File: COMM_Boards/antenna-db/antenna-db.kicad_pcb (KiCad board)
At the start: 4 copper layers, 90.2 x 95.9 mm, 5 parts, among them J1 PC104_Connector

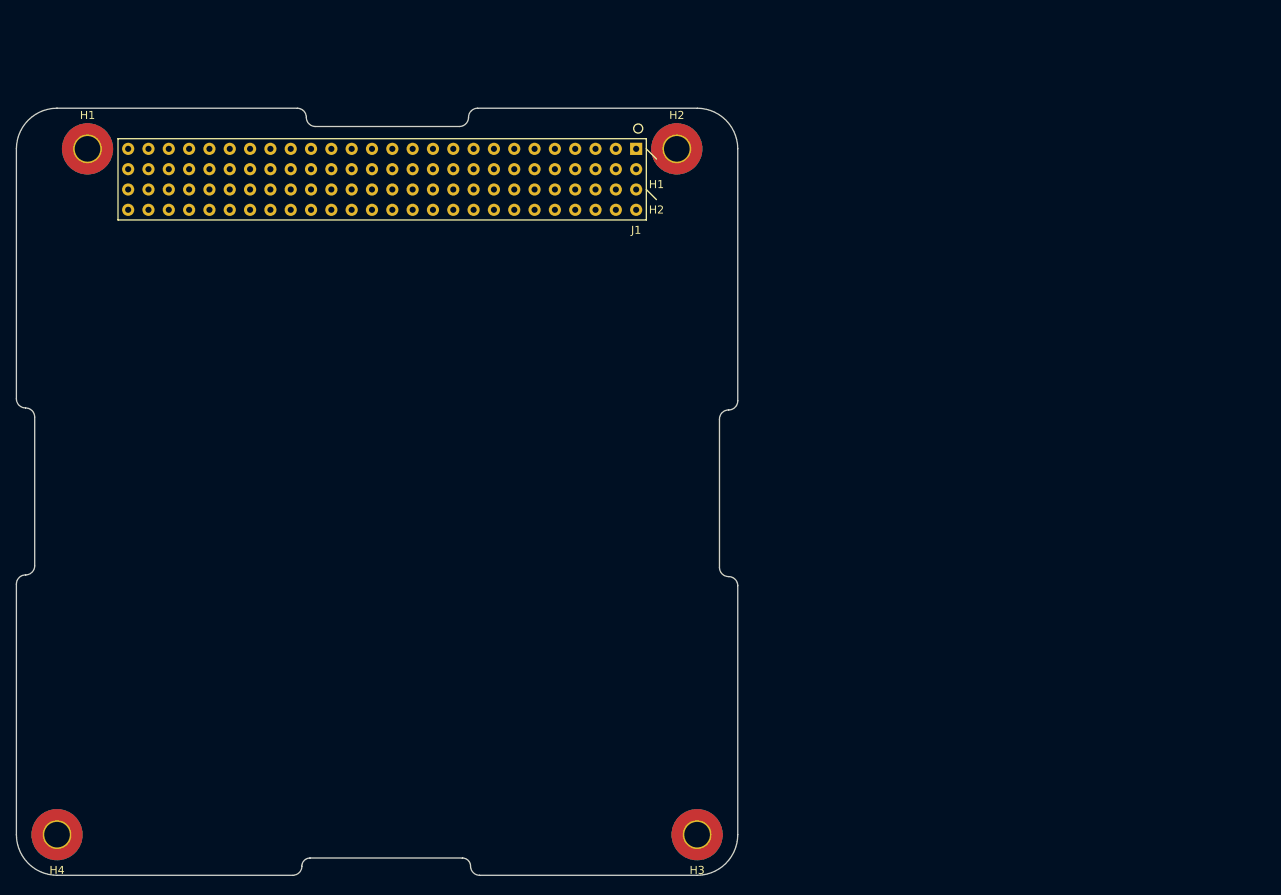
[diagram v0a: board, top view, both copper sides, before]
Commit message: COMM: antt-dbd: map mounting holes to pcb layout
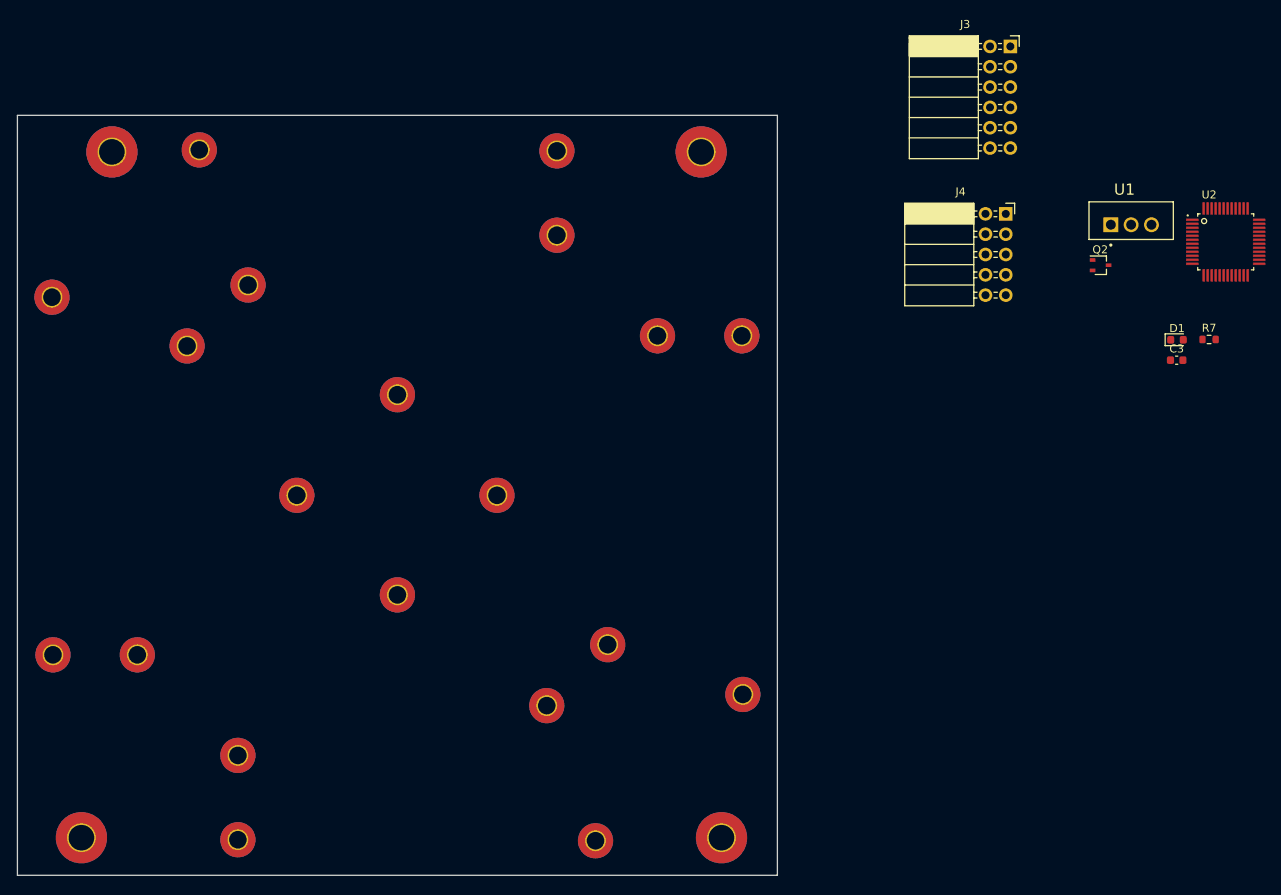
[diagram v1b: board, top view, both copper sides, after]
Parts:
- removed J1: PC104_Connector, pc104-connector:pc104-connector
- added C3: 0.1uF, Capacitor_SMD:C_0603_1608Metric, F.Cu at (254.3, 78.5)
- added D1: RED, Diode_SMD:D_0603_1608Metric, F.Cu at (254.3, 75.9)
- added H10: 2.1mm, MountingHole:MountingHole_2.2mm_M2_Pad_TopBottom, F.Cu at (200.0, 120.3)
- added H11: 2.1mm, MountingHole:MountingHole_2.2mm_M2_Pad_TopBottom, F.Cu at (175.5, 121.7)
- added H12: 2.1mm, MountingHole:MountingHole_2.2mm_M2_Pad_TopBottom, F.Cu at (183.1, 114.0)
- added H13: 2.1mm, MountingHole:MountingHole_2.2mm_M2_Pad_TopBottom, F.Cu at (169.3, 95.4)
- added H14: 2.1mm, MountingHole:MountingHole_2.2mm_M2_Pad_TopBottom, F.Cu at (156.8, 107.8)
- added H15: 2.1mm, MountingHole:MountingHole_2.2mm_M2_Pad_TopBottom, F.Cu at (156.8, 82.8)
- added H16: 2.1mm, MountingHole:MountingHole_2.2mm_M2_Pad_TopBottom, F.Cu at (113.7, 70.6)
- added H17: 2.1mm, MountingHole:MountingHole_2.2mm_M2_Pad_TopBottom, F.Cu at (144.3, 95.4)
- added H18: 2.1mm, MountingHole:MountingHole_2.2mm_M2_Pad_TopBottom, F.Cu at (132.1, 52.2)
- added H19: 2.1mm, MountingHole:MountingHole_2.2mm_M2_Pad_TopBottom, F.Cu at (130.6, 76.7)
- added H20: 2.1mm, MountingHole:MountingHole_2.2mm_M2_Pad_TopBottom, F.Cu at (138.2, 69.1)
- added H21: 2.1mm, MountingHole:MountingHole_2.2mm_M2_Pad_TopBottom, F.Cu at (199.9, 75.4)
- added H22: 2.1mm, MountingHole:MountingHole_2.2mm_M2_Pad_TopBottom, F.Cu at (176.8, 52.3)
- added H23: 2.1mm, MountingHole:MountingHole_2.2mm_M2_Pad_TopBottom, F.Cu at (176.8, 62.9)
- added H24: 2.1mm, MountingHole:MountingHole_2.2mm_M2_Pad_TopBottom, F.Cu at (189.4, 75.4)
- added H5: 2.1mm, MountingHole:MountingHole_2.2mm_M2_Pad_TopBottom, F.Cu at (136.9, 127.9)
- added H6: 2.1mm, MountingHole:MountingHole_2.2mm_M2_Pad_TopBottom, F.Cu at (136.9, 138.4)
- added H7: 2.1mm, MountingHole:MountingHole_2.2mm_M2_Pad_TopBottom, F.Cu at (124.3, 115.3)
- added H8: 2.1mm, MountingHole:MountingHole_2.2mm_M2_Pad_TopBottom, F.Cu at (113.8, 115.3)
- added H9: 2.1mm, MountingHole:MountingHole_2.2mm_M2_Pad_TopBottom, F.Cu at (181.6, 138.6)
- added J3: System Test Connector, Connector_PinSocket_2.54mm:PinSocket_2x06_P2.54mm_Horizontal, F.Cu at (233.5, 39.3)
- added J4: Programming Header, Connector_PinSocket_2.54mm:PinSocket_2x05_P2.54mm_Horizontal, F.Cu at (232.9, 60.2)
- added Q2: BC817W, Package_TO_SOT_SMD:SOT-323_SC-70, F.Cu at (244.7, 66.6)
- added R7: 2.2k, Resistor_SMD:R_0603_1608Metric, F.Cu at (258.3, 75.9)
- added U1: LM338T, qset-footprints:TO254P1054X470X1955-3, F.Cu at (248.6, 61.6)
- added U2: STM32F030CCT6, qset-footprints:QFP50P900X900X160-48N, F.Cu at (260.4, 63.7)
- moved H1 3.07 mm to (121.2, 52.5)
- moved H2 3.07 mm to (194.8, 52.5)
- moved H3 3.07 mm to (197.4, 138.2)
- moved H4 3.07 mm to (117.3, 138.2)
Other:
- board size 90.2 x 95.9 mm -> 95 x 95 mm

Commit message: include SC4216 regulator
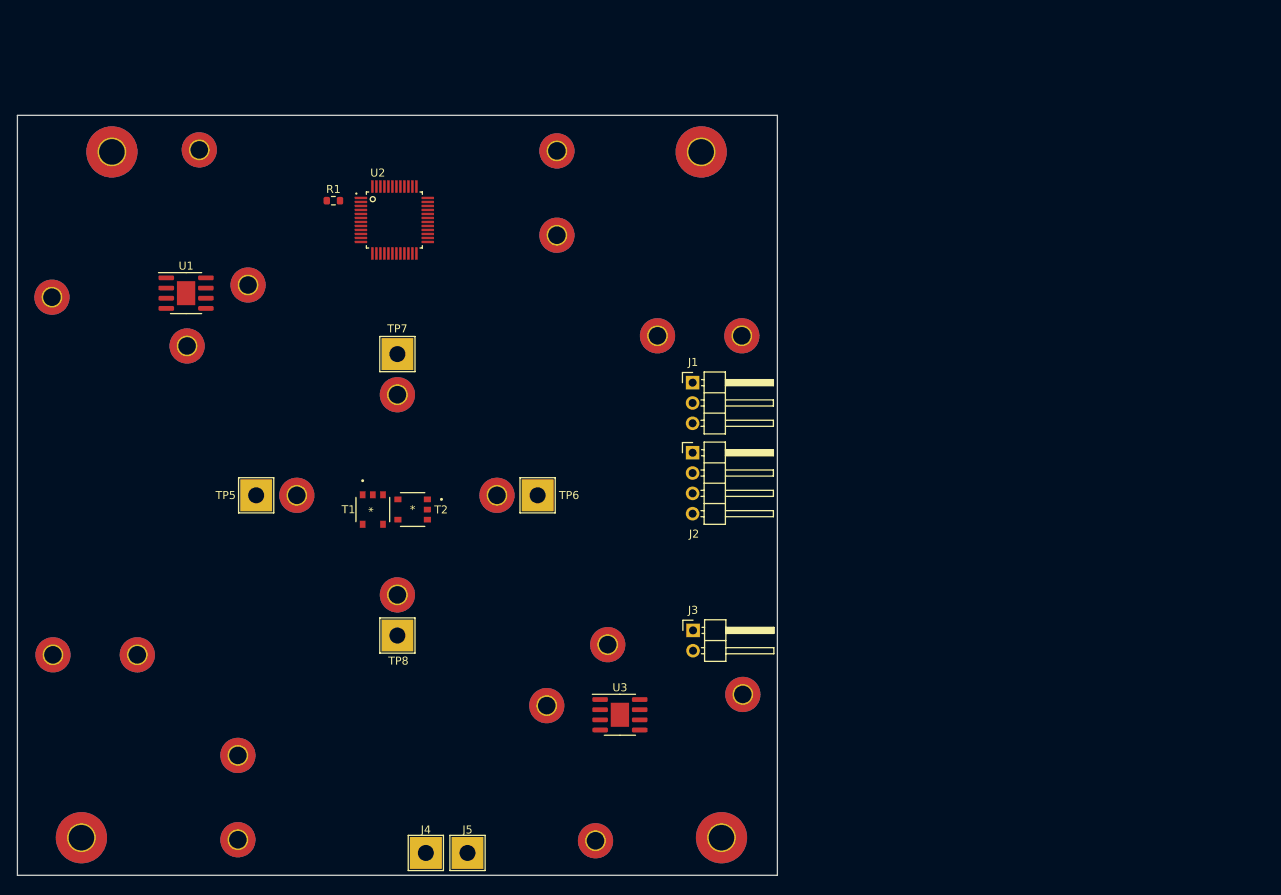
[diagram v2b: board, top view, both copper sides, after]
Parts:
- removed C3: 0.1uF, Capacitor_SMD:C_0603_1608Metric
- removed D1: RED, Diode_SMD:D_0603_1608Metric
- removed Q2: BC817W, Package_TO_SOT_SMD:SOT-323_SC-70
- removed R7: 2.2k, Resistor_SMD:R_0603_1608Metric
- added J1: Conn_01x03, Connector_PinHeader_2.54mm:PinHeader_1x03_P2.54mm_Horizontal, F.Cu at (193.7, 81.3)
- added J2: Conn_01x04, Connector_PinHeader_2.54mm:PinHeader_1x04_P2.54mm_Horizontal, F.Cu at (193.7, 90.1)
- added J5: Conn_Coaxial, TestPoint:TestPoint_THTPad_4.0x4.0mm_Drill2.0mm, F.Cu at (165.6, 140.1)
- added R1: 100k, Resistor_SMD:R_0603_1608Metric, F.Cu at (148.8, 58.5)
- added T1: MABA-007159-000000, qset-footprints:MABA-007159-000000, F.Cu at (153.8, 97.2)
- added T2: MABA-007159-000000, qset-footprints:MABA-007159-000000, F.Cu at (158.8, 97.2)
- added TP5: TestPoint, TestPoint:TestPoint_THTPad_4.0x4.0mm_Drill2.0mm, F.Cu at (139.2, 95.4)
- added TP6: TestPoint, TestPoint:TestPoint_THTPad_4.0x4.0mm_Drill2.0mm, F.Cu at (174.4, 95.4)
- added TP7: TestPoint, TestPoint:TestPoint_THTPad_4.0x4.0mm_Drill2.0mm, F.Cu at (156.8, 77.7)
- added TP8: TestPoint, TestPoint:TestPoint_THTPad_4.0x4.0mm_Drill2.0mm, F.Cu at (156.8, 112.9)
- added U3: SC4216HSETRT, Package_SO:SOIC-8-1EP_3.9x4.9mm_P1.27mm_EP2.29x3mm, F.Cu at (184.7, 122.8)
- J3: value System Test Connector -> Conn_01x02_Male; footprint Connector_PinSocket_2.54mm:PinSocket_2x06_P2.54mm_Horizontal -> Connector_PinHeader_2.54mm:PinHeader_1x02_P2.54mm_Horizontal
- J4: value Programming Header -> Conn_Coaxial; footprint Connector_PinSocket_2.54mm:PinSocket_2x05_P2.54mm_Horizontal -> TestPoint:TestPoint_THTPad_4.0x4.0mm_Drill2.0mm
- U1: value LM338T -> SC4216HSETRT; footprint qset-footprints:TO254P1054X470X1955-3 -> Package_SO:SOIC-8-1EP_3.9x4.9mm_P1.27mm_EP2.29x3mm
- moved U1 118.4 mm to (130.4, 70.1)
- moved J4 107.9 mm to (160.4, 140.1)
- moved U2 104.0 mm to (156.5, 61.0)
- moved J3 83.1 mm to (193.8, 112.3)
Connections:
- J3 pad 1: +3V3 -> POWER_EN_R
- J3 pad 2: +3V3 -> GND
- J4 pad 1: NRST -> Net-(J4-Pad1)
- U1 pad 1: GND -> unconnected-(U1-Pad1)
- U1 pad 2: Net-(Q2-Pad3) -> unconnected-(U1-Pad2)
- U1 pad 3: 3V3 -> unconnected-(U1-Pad3)
- U2 pad 7: /NRST -> NRST

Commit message: COMM: antt-dbd: finish deployment detection and arming control
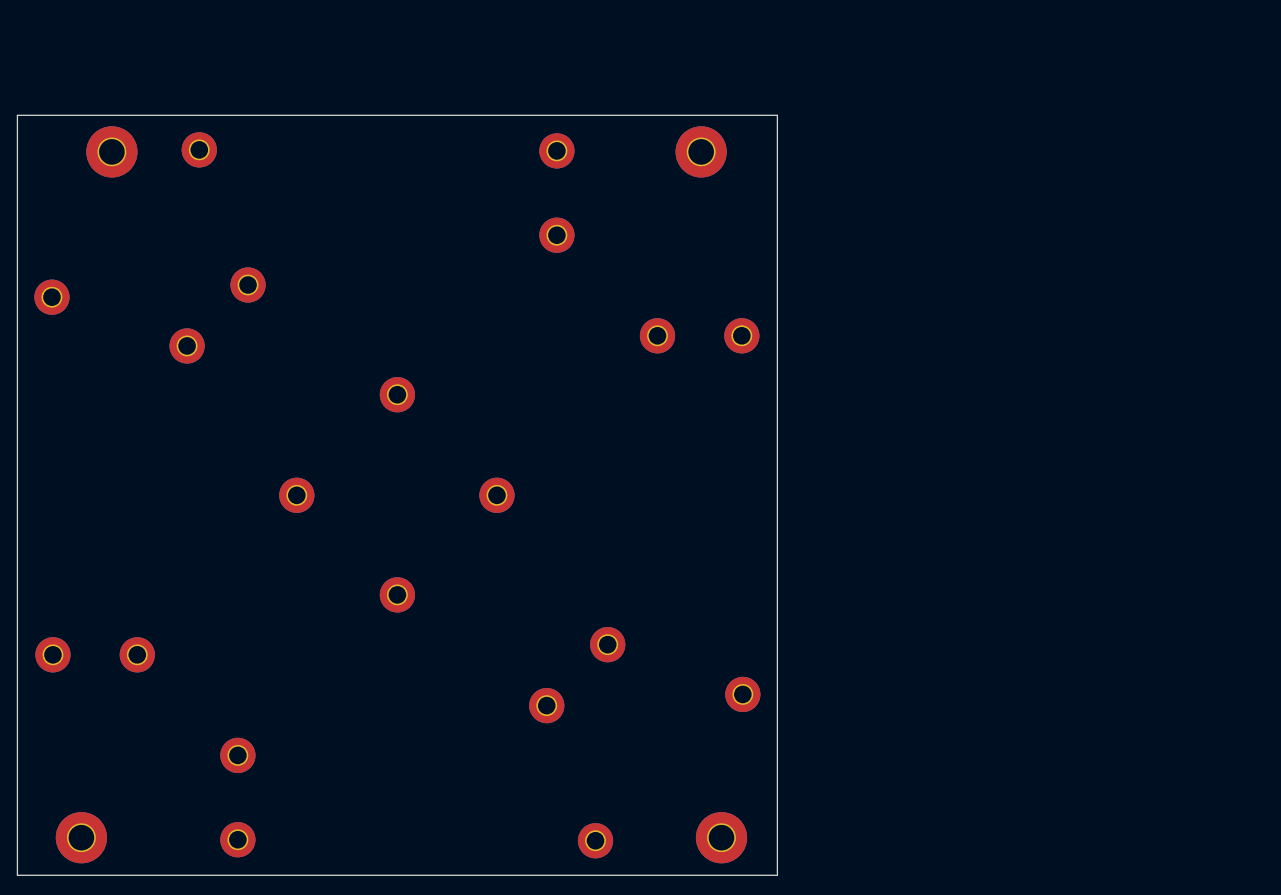
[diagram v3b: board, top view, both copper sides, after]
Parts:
- removed J1: Conn_01x03, Connector_PinHeader_2.54mm:PinHeader_1x03_P2.54mm_Horizontal
- removed J2: Conn_01x04, Connector_PinHeader_2.54mm:PinHeader_1x04_P2.54mm_Horizontal
- removed J3: Conn_01x02_Male, Connector_PinHeader_2.54mm:PinHeader_1x02_P2.54mm_Horizontal
- removed J4, J5: Conn_Coaxial, TestPoint:TestPoint_THTPad_4.0x4.0mm_Drill2.0mm
- removed R1: 100k, Resistor_SMD:R_0603_1608Metric
- removed T1, T2: MABA-007159-000000, qset-footprints:MABA-007159-000000
- removed TP5, TP6, TP7, TP8: TestPoint, TestPoint:TestPoint_THTPad_4.0x4.0mm_Drill2.0mm
- removed U1, U3: SC4216HSETRT, Package_SO:SOIC-8-1EP_3.9x4.9mm_P1.27mm_EP2.29x3mm
- removed U2: STM32F030CCT6, qset-footprints:QFP50P900X900X160-48N

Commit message: COMM: antt-dbd: begin layout
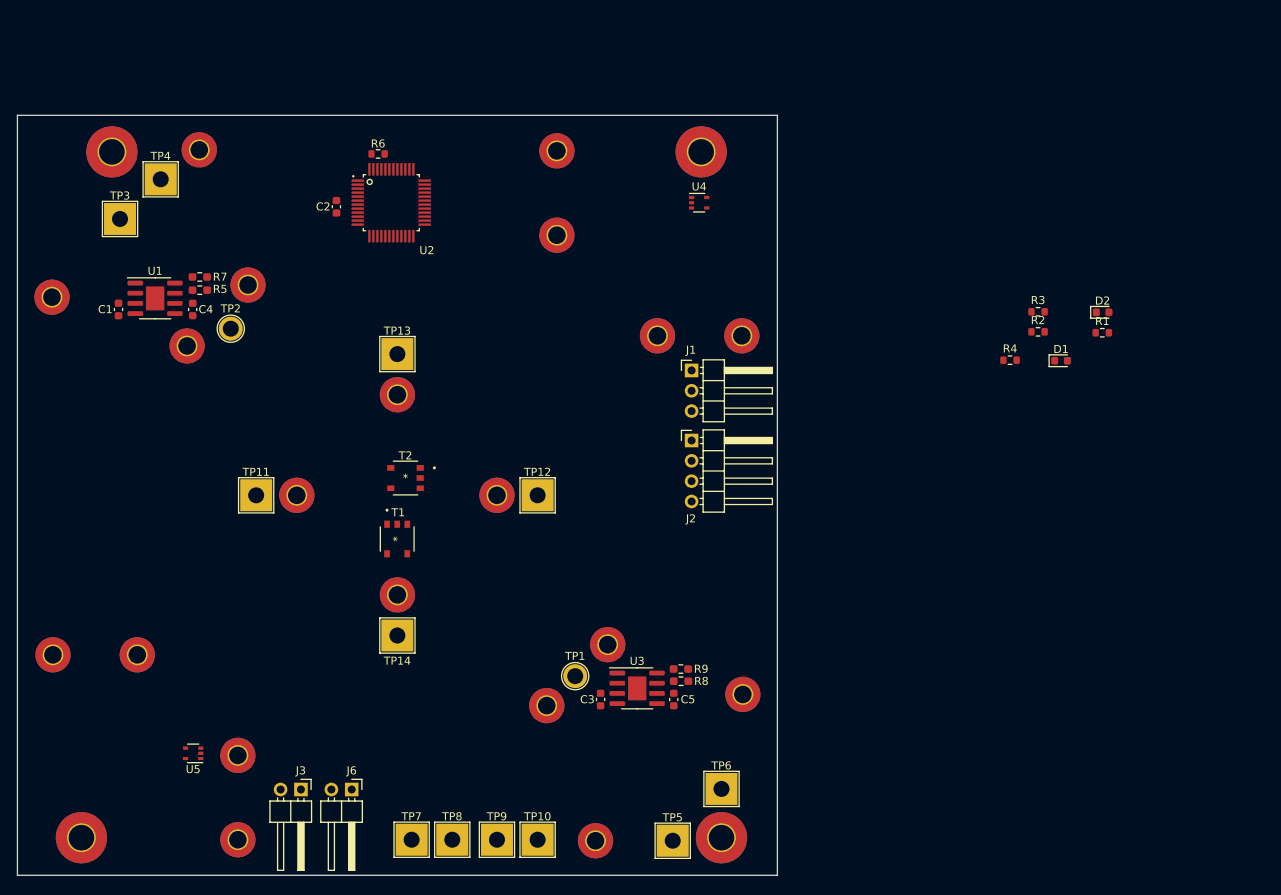
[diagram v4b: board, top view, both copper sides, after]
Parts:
- added C1: 0.1u, Capacitor_SMD:C_0603_1608Metric, F.Cu at (122.0, 72.1)
- added C2: 100u, Capacitor_SMD:C_0603_1608Metric, F.Cu at (149.2, 59.3)
- added C3: 0.1u, Capacitor_SMD:C_0603_1608Metric, F.Cu at (182.2, 120.9)
- added C4: 0.1u, Capacitor_SMD:C_0603_1608Metric, F.Cu at (131.3, 72.1)
- added C5: 0.1u, Capacitor_SMD:C_0603_1608Metric, F.Cu at (191.4, 120.9)
- added D1: YLW, LED_SMD:LED_0603_1608Metric, F.Cu at (239.8, 78.6)
- added D2: YLW, LED_SMD:LED_0603_1608Metric, F.Cu at (245.0, 72.5)
- added J1: Conn_01x03, Connector_PinHeader_2.54mm:PinHeader_1x03_P2.54mm_Horizontal, F.Cu at (193.6, 79.8)
- added J2: Conn_01x04, Connector_PinHeader_2.54mm:PinHeader_1x04_P2.54mm_Horizontal, F.Cu at (193.6, 88.5)
- added J3: Conn_01x02_Male, Connector_PinHeader_2.54mm:PinHeader_1x02_P2.54mm_Horizontal, F.Cu at (144.8, 132.2)
- added J6: Conn_01x02_Male, Connector_PinHeader_2.54mm:PinHeader_1x02_P2.54mm_Horizontal, F.Cu at (151.1, 132.2)
- added R1: 2k2, Resistor_SMD:R_0603_1608Metric, F.Cu at (245.0, 75.1)
- added R2: 2k2, Resistor_SMD:R_0603_1608Metric, F.Cu at (236.9, 74.9)
- added R3: 100k, Resistor_SMD:R_0603_1608Metric, F.Cu at (236.9, 72.4)
- added R4: 100k, Resistor_SMD:R_0603_1608Metric, F.Cu at (233.4, 78.5)
- added R5: DNP, Resistor_SMD:R_0603_1608Metric_Pad0.98x0.95mm_HandSolder, F.Cu at (132.1, 69.7)
- added R6: 10k, Resistor_SMD:R_0603_1608Metric, F.Cu at (154.4, 52.7)
- added R7: 0, Resistor_SMD:R_0603_1608Metric_Pad0.98x0.95mm_HandSolder, F.Cu at (132.1, 68.1)
- added R8: DNP, Resistor_SMD:R_0603_1608Metric_Pad0.98x0.95mm_HandSolder, F.Cu at (192.3, 118.6)
- added R9: 0, Resistor_SMD:R_0603_1608Metric_Pad0.98x0.95mm_HandSolder, F.Cu at (192.3, 117.1)
- added T1: MABA-007159-000000, qset-footprints:MABA-007159-000000, F.Cu at (156.8, 100.8)
- added T2: MABA-007159-000000, qset-footprints:MABA-007159-000000, F.Cu at (157.9, 93.2)
- added TP1: PWR_EN_144, TestPoint:TestPoint_Plated_Hole_D2.0mm, F.Cu at (179.1, 118.0)
- added TP10: 434 Coax Sleeve Connection, TestPoint:TestPoint_THTPad_4.0x4.0mm_Drill2.0mm, F.Cu at (174.4, 138.4)
- added TP11: 144 Atenna Arm +, TestPoint:TestPoint_THTPad_4.0x4.0mm_Drill2.0mm, F.Cu at (139.2, 95.4)
- added TP12: 144 Atenna Arm -, TestPoint:TestPoint_THTPad_4.0x4.0mm_Drill2.0mm, F.Cu at (174.4, 95.4)
- added TP13: 434 Atenna Arm +, TestPoint:TestPoint_THTPad_4.0x4.0mm_Drill2.0mm, F.Cu at (156.8, 77.7)
- added TP14: 434 Atenna Arm -, TestPoint:TestPoint_THTPad_4.0x4.0mm_Drill2.0mm, F.Cu at (156.8, 112.9)
- added TP2: PWR_EN_144, TestPoint:TestPoint_Plated_Hole_D2.0mm, F.Cu at (136.0, 74.5)
- added TP3: TestPoint, TestPoint:TestPoint_THTPad_4.0x4.0mm_Drill2.0mm, F.Cu at (122.2, 60.8)
- added TP4: TestPoint, TestPoint:TestPoint_THTPad_4.0x4.0mm_Drill2.0mm, F.Cu at (127.3, 55.9)
- added TP5: TestPoint, TestPoint:TestPoint_THTPad_4.0x4.0mm_Drill2.0mm, F.Cu at (191.3, 138.6)
- added TP6: TestPoint, TestPoint:TestPoint_THTPad_4.0x4.0mm_Drill2.0mm, F.Cu at (197.4, 132.1)
- added TP7: 144 Coax Pin Connection, TestPoint:TestPoint_THTPad_4.0x4.0mm_Drill2.0mm, F.Cu at (158.6, 138.4)
- added TP8: 144 Coax Sleeve Connection, TestPoint:TestPoint_THTPad_4.0x4.0mm_Drill2.0mm, F.Cu at (163.7, 138.4)
- added TP9: 434 Coax Pin Connection, TestPoint:TestPoint_THTPad_4.0x4.0mm_Drill2.0mm, F.Cu at (169.3, 138.4)
- added U1: SC4216HSETRT, Package_SO:SOIC-8-1EP_3.9x4.9mm_P1.27mm_EP2.29x3mm, F.Cu at (126.6, 70.8)
- added U2: STM32F030CCT6, qset-footprints:QFP50P900X900X160-48N, F.Cu at (156.1, 58.8)
- added U3: SC4216HSETRT, Package_SO:SOIC-8-1EP_3.9x4.9mm_P1.27mm_EP2.29x3mm, F.Cu at (186.8, 119.5)
- added U4: 74AHC1G08, Package_TO_SOT_SMD:SOT-353_SC-70-5, F.Cu at (194.6, 58.8)
- added U5: 74AHC1G08, Package_TO_SOT_SMD:SOT-353_SC-70-5, F.Cu at (131.3, 127.6)
